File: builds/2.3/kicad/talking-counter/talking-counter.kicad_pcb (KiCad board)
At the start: 2 copper layers, 94 x 63.5 mm, 60 parts, among them IC1 TLV3501AIDR, IC2 LM4862MX_NOPB, J1 Conn_Coaxial, J2 PROG, J3 UJ2-MIBH-G-SMT-TR, SW1 SW_MEC_5E, U1 FT231XS, U2 AP2112K-3.3, U3 AVR64DD32, U4 FT5HV

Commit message: layout pcb
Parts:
- moved H4 8.03 mm to (132.3, 107.2)
- moved H2 7.62 mm to (132.3, 55.4)
- moved H3 2.54 mm to (55.6, 107.2)
- moved SW1 0.05 mm to (121.9, 101.1)
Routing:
- net Net-(D6-K): track 1.62 -> 24.6 mm, vias 1 -> 2
- net (no net): track 0.51 -> 0.00 mm
- net GND: track 45.6 -> 45.7 mm, vias 24 -> 23
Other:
- board size 94 x 63.5 mm -> 86.4 x 61 mm
- board text added: "INPUT"
- board text added: "SPEAK"
- board text added: "Talking Frequency Meter 2.3"
- board text added: "VOLUME"
- board text added: "optional"

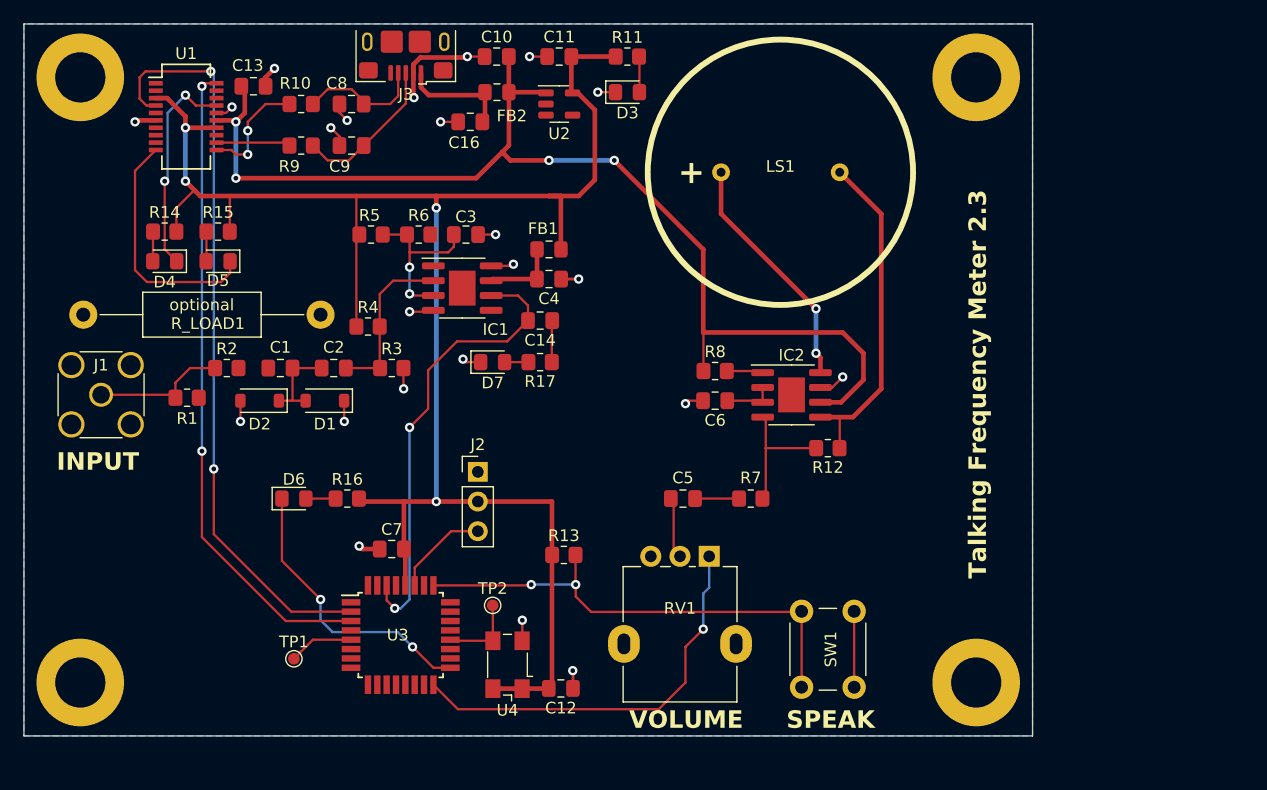
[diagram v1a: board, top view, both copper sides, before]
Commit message: PCB updates based on DRC
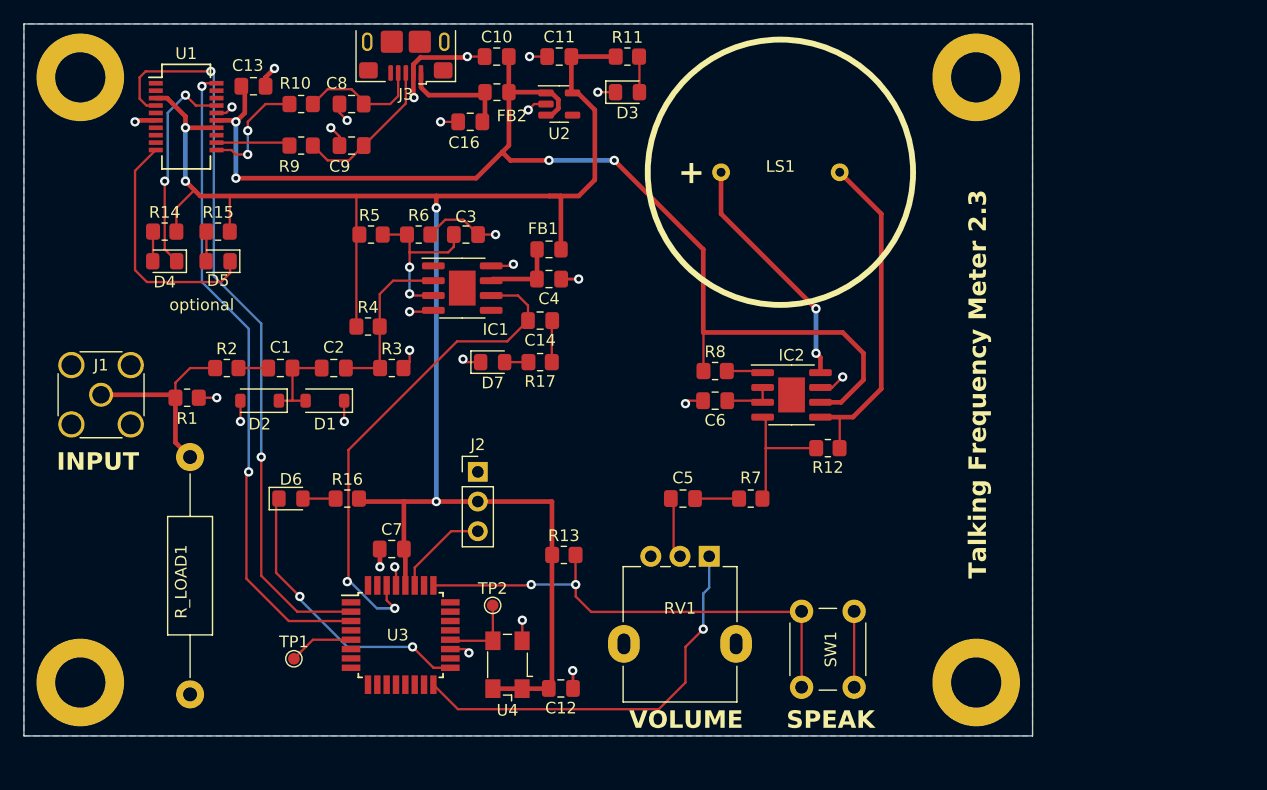
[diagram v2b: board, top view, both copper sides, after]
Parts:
- moved R_LOAD1 15.2 mm to (65.0, 87.9), turned to -90 degrees
- moved D6 0.25 mm to (73.7, 91.4)
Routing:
- net GND: track 45.7 -> 57.1 mm, vias 23 -> 27
- net Net-(J1-In): track 11.7 -> 17.3 mm
- net COMP_OUT: track 39.2 -> 43.3 mm
- net +5V: track 97.7 -> 101.0 mm
- net Net-(C1-Pad2): track 0.00 -> 2.55 mm

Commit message: Create gerber.zip
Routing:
- net DAC: track 35.0 -> 34.1 mm
- net Net-(U3-PF5): track 42.2 -> 41.6 mm
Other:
- board text added: "JLCJLCJLCJLC"
